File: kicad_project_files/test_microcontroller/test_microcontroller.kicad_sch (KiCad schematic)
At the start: 43 parts, among them J1 USB_C_Receptacle_USB2.0, SW1 SW_Push, SW2 SW_Push, SW3 SW_Push, SW4 SW_Push, SW5 SW_Push, SW6 SW_Push, SW7 SW_Push, SW8 SW_Push, SW9 SW_Push, U1 ATmega32U4-A, Y1 16mhz

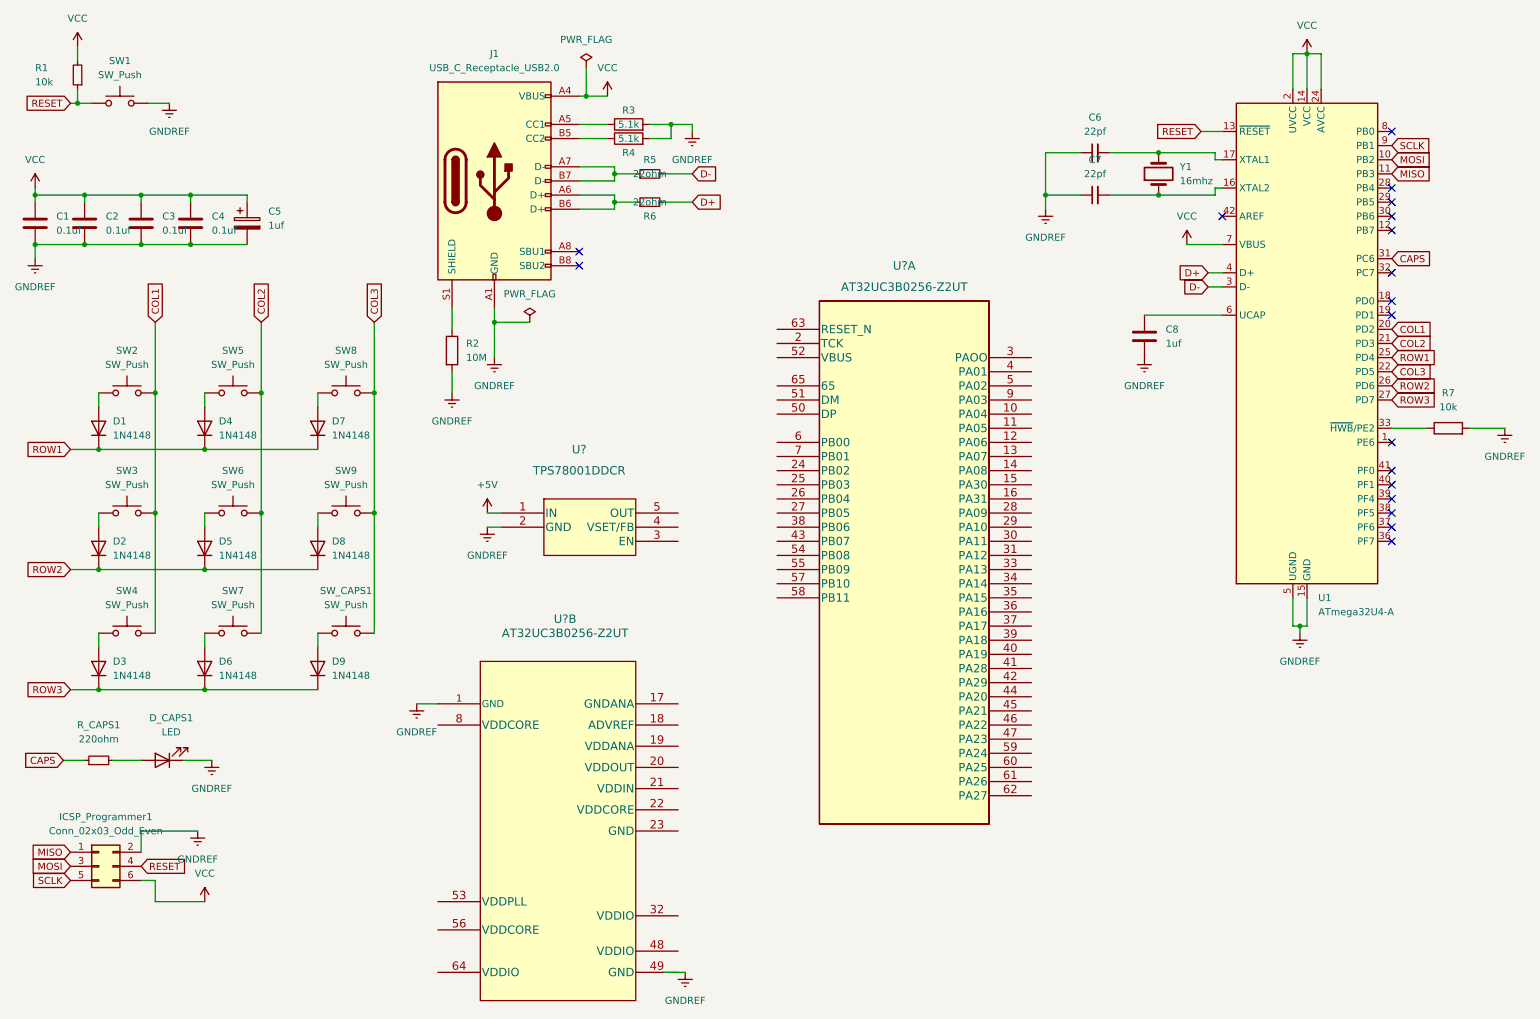
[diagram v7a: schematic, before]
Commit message: new voltage reg
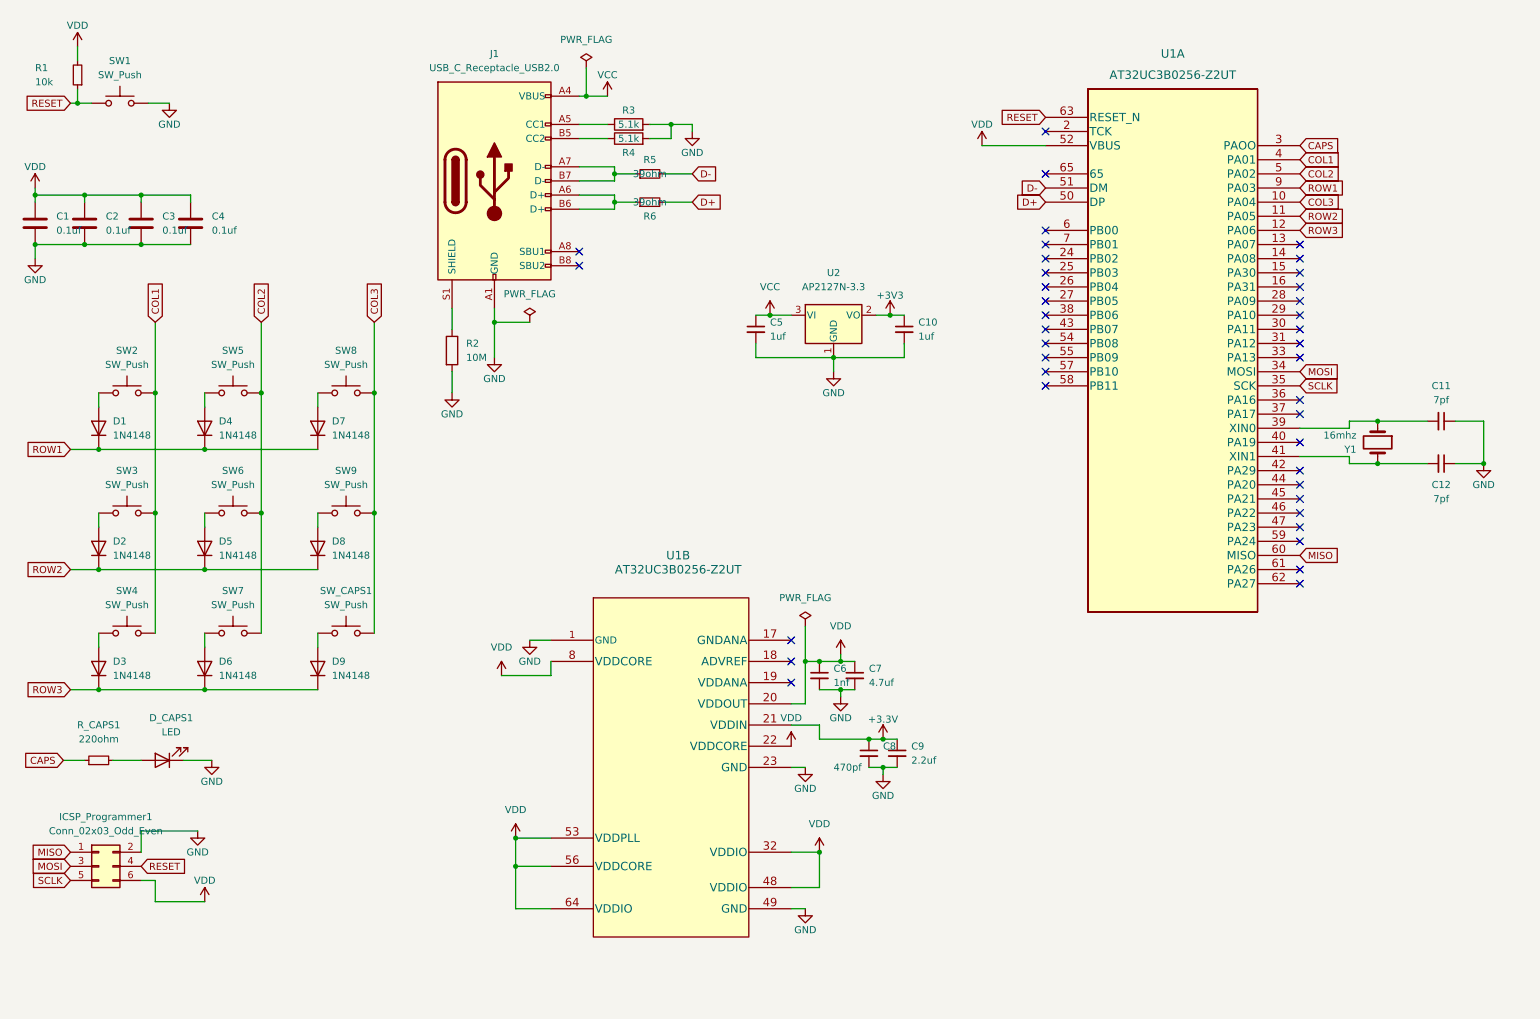
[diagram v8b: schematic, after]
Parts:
- removed C5: 1uf, Capacitor_THT:CP_Radial_D4.0mm_P1.50mm, symbol Device:C_Polarized
- removed C8: 1uf, Capacitor_THT:CP_Radial_D4.0mm_P1.50mm, symbol Device:C
- removed R7: 10k, Resistor_THT:R_Axial_DIN0204_L3.6mm_D1.6mm_P5.08mm_Horizontal, symbol Device:R
- removed U1: ATmega32U4-A, Package_QFP:TQFP-44_10x10mm_P0.8mm, symbol MCU_Microchip_ATmega:ATmega32U4-A
- removed U?: TPS78001DDCR, DDC5, symbol TPS780xx:TPS78001DDCR
- added C10, C5: 1uf, Capacitor_THT:CP_Radial_D4.0mm_P1.50mm, symbol Device:C_Small
- added C11, C12: 7pf, Capacitor_THT:C_Disc_D3.0mm_W1.6mm_P2.50mm, symbol Device:C_Small
- added C8: 470pf, symbol Device:C_Small
- added C9: 2.2uf, symbol Device:C_Small
- added U2: AP2127N-3.3, Package_TO_SOT_SMD:SOT-23, symbol Regulator_Linear:AP2127N-3.3
- C6: value 22pf -> 1nf; footprint Capacitor_THT:C_Disc_D3.0mm_W1.6mm_P2.50mm -> (none)
- C7: value 22pf -> 4.7uf; footprint Capacitor_THT:C_Disc_D3.0mm_W1.6mm_P2.50mm -> (none)
- R5, R6: value 22ohm -> 39ohm
- gave numbers to parts that had none: 1
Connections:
- net CAPS: now also U1.3 (PAOO)
- net COL1: now also U1.4 (PA01)
- net COL2: now also U1.5 (PA02)
- net COL3: now also U1.10 (PA04)
- net D+: now also U1.50 (DP)
- net D-: now also U1.51 (DM)
- net MISO: now also U1.60 (MISO)
- net MOSI: now also U1.34 (MOSI)
- net RESET: now also U1.63 (RESET_N)
- net ROW1: now also U1.9 (PA03)
- net ROW2: now also U1.11 (PA05)
- net ROW3: now also U1.12 (PA06)
- net SCLK: now also U1.35 (SCK)
- net VCC: now also C5.1, U2.3 (VI); no longer C1.1, C2.1, C3.1, C4.1, ICSP_Programmer1.6 (Pin_6), R1.2
- net at Y1.1: now also U1.39 (XIN0), C11.2; no longer C7.2
- net at Y1.2: now also U1.41 (XIN1), C12.2; no longer C6.2
- net VDD: now reaches U1.20 (VDDOUT)
- net VDD: now also C1.1, C2.1, C3.1, C4.1, C6.1, C7.1, ICSP_Programmer1.6 (Pin_6), R1.2, U1.22 (VDDCORE), U1.32 (VDDIO), U1.48 (VDDIO), U1.52 (VBUS), U1.53 (VDDPLL), U1.56 (VDDCORE), U1.64 (VDDIO), U1.8 (VDDCORE)
- net +3V3: now reaches U1.21 (VDDIN)
- net +3V3: now also C10.1, C8.1, C9.1, U2.2 (VO)
- net GND: now reaches U1.23 (GND)
- net GND: now also C1.2, C2.2, C3.2, C4.2, C6.2, C7.2, D_CAPS1.1 (K), ICSP_Programmer1.2 (Pin_2), J1.A1 (GND), J1.A12 (GND), J1.B1 (GND), J1.B12 (GND), R2.2, R3.2, R4.2, SW1.2, U1.1 (GND), U1.49 (GND), C10.2, C11.1, C12.1, C5.2, C8.2, C9.2, U2.1 (GND)
- removed net GNDREF: C1.2, C2.2, C3.2, C4.2, C6.1, C7.1, D_CAPS1.1 (K), ICSP_Programmer1.2 (Pin_2), J1.A1 (GND), J1.A12 (GND), J1.B1 (GND), J1.B12 (GND), R2.2, R3.2, R4.2, SW1.2, U1.1 (GND)
- no-connect marks 18 -> 39
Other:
- moved on the sheet: U1A, U1B
